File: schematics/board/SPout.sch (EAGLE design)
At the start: 38 parts

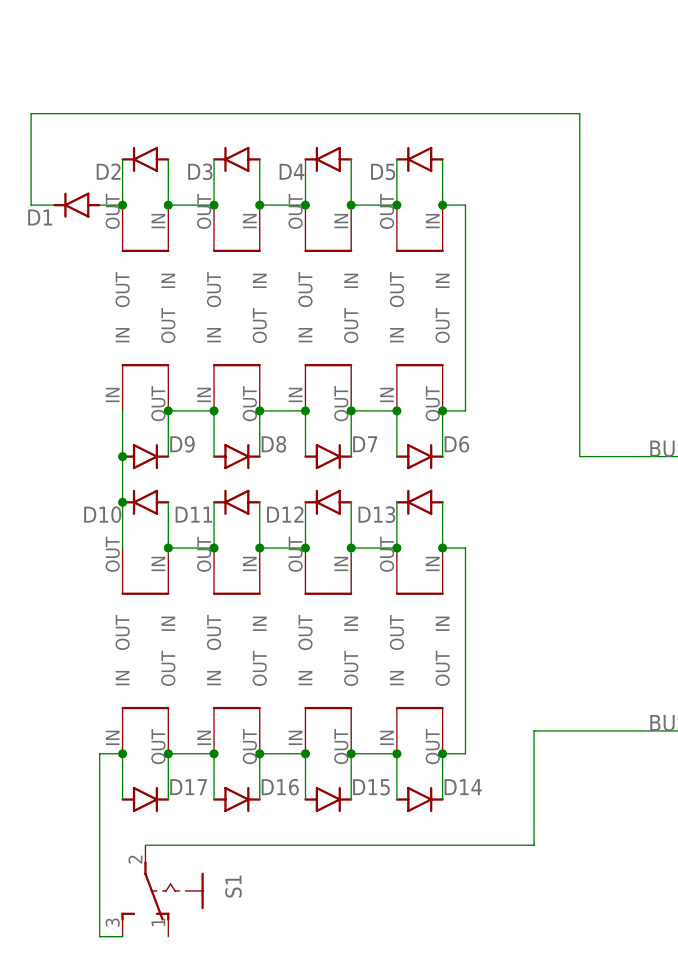
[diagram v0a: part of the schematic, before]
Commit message: Плата СП изменена для возможности подключения 2 вариантов ФЭПов
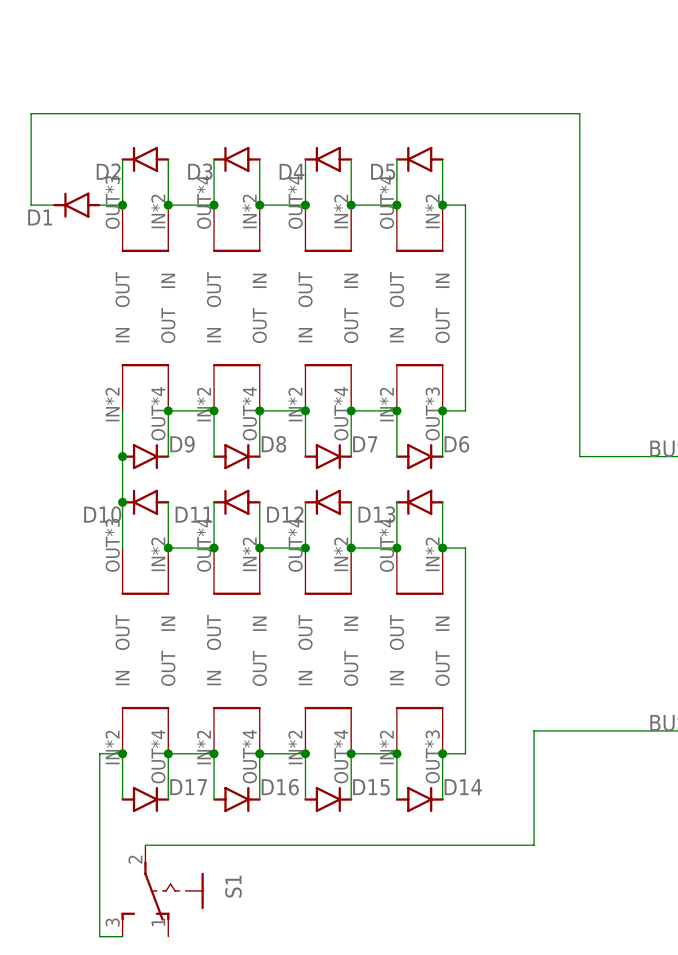
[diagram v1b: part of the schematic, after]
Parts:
- SOL1, SOL10, SOL11, SOL13, SOL14, SOL15, SOL2, SOL3, SOL5, SOL6, SOL7, SOL9: value SOLAR_0 -> SOLAR-2_0; device CanCubeSat:SOLAR_0 -> CanCubeSat:SOLAR-2_0
- SOL12, SOL16, SOL4, SOL8: value SOLAR_1 -> SOLAR-2_1; device CanCubeSat:SOLAR_1 -> CanCubeSat:SOLAR-2_1
- U$6: value GRAFITGRAFIT3_1 -> GRAFITGRAFIT4_2; device CanCubeSat:GRAFITGRAFIT3_1 -> CanCubeSat:GRAFITGRAFIT4_2
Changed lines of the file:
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@@
 <parts>
 <part name="D1" library="diode" library_urn="urn:adsk.eagle:library:210" deviceset="MBR0520LT" device="" package3d_urn="urn:adsk.eagle:package:43420/1"/>
-<part name="SOL1" library="CanCubeSat" deviceset="SOLAR" device="_0"/>
-<part name="SOL2" library="CanCubeSat" deviceset="SOLAR" device="_0"/>
-<part name="SOL3" library="CanCubeSat" deviceset="SOLAR" device="_0"/>
-<part name="SOL5" library="CanCubeSat" deviceset="SOLAR" device="_0"/>
-<part name="SOL6" library="CanCubeSat" deviceset="SOLAR" device="_0"/>
-<part name="SOL7" library="CanCubeSat" deviceset="SOLAR" device="_0"/>
-<part name="SOL9" library="CanCubeSat" deviceset="SOLAR" device="_0"/>
-<part name="SOL10" library="CanCubeSat" deviceset="SOLAR" device="_0"/>
-<part name="SOL11" library="CanCubeSat" deviceset="SOLAR" device="_0"/>
-<part name="SOL13" library="CanCubeSat" deviceset="SOLAR" device="_0"/>
-<part name="SOL14" library="CanCubeSat" deviceset="SOLAR" device="_0"/>
-<part name="SOL15" library="CanCubeSat" deviceset="SOLAR" device="_0"/>
-<part name="SOL16" library="CanCubeSat" deviceset="SOLAR" device="_1"/>
-<part name="SOL12" library="CanCubeSat" deviceset="SOLAR" device="_1"/>
-<part name="SOL8" library="CanCubeSat" deviceset="SOLAR" device="_1"/>
-<part name="SOL4" library="CanCubeSat" deviceset="SOLAR" device="_1"/>
+<part name="SOL1" library="CanCubeSat" deviceset="SOLAR-2" device="_0"/>
+<part name="SOL2" library="CanCubeSat" deviceset="SOLAR-2" device="_0"/>
+<part name="SOL3" library="CanCubeSat" deviceset="SOLAR-2" device="_0"/>
+<part name="SOL5" library="CanCubeSat" deviceset="SOLAR-2" device="_0"/>
+<part name="SOL6" library="CanCubeSat" deviceset="SOLAR-2" device="_0"/>
+<part name="SOL7" library="CanCubeSat" deviceset="SOLAR-2" device="_0"/>
+<part name="SOL9" library="CanCubeSat" deviceset="SOLAR-2" device="_0"/>
+<part name="SOL10" library="CanCubeSat" deviceset="SOLAR-2" device="_0"/>
+<part name="SOL11" library="CanCubeSat" deviceset="SOLAR-2" device="_0"/>
+<part name="SOL13" library="CanCubeSat" deviceset="SOLAR-2" device="_0"/>
+<part name="SOL14" library="CanCubeSat" deviceset="SOLAR-2" device="_0"/>
+<part name="SOL15" library="CanCubeSat" deviceset="SOLAR-2" device="_0"/>
+<part name="SOL16" library="CanCubeSat" deviceset="SOLAR-2" device="_1"/>
+<part name="SOL12" library="CanCubeSat" deviceset="SOLAR-2" device="_1"/>
+<part name="SOL8" library="CanCubeSat" deviceset="SOLAR-2" device="_1"/>
+<part name="SOL4" library="CanCubeSat" deviceset="SOLAR-2" device="_1"/>
 <part name="S1" library="CanCubeSat" deviceset="255SB" device="" package3d_urn="urn:adsk.eagle:package:27679/1"/>
 <part name="R1_2K7" library="rcl" library_urn="urn:adsk.eagle:library:334" deviceset="R-US_" device="R0603" package3d_urn="urn:adsk.eagle:package:23555/3" value="2k7"/>
@@
 <part name="D16" library="diode" library_urn="urn:adsk.eagle:library:210" deviceset="MBR0520LT" device="" package3d_urn="urn:adsk.eagle:package:43420/1"/>
 <part name="D17" library="diode" library_urn="urn:adsk.eagle:library:210" deviceset="MBR0520LT" device="" package3d_urn="urn:adsk.eagle:package:43420/1"/>
-<part name="U$6" library="CanCubeSat" deviceset="GRAFIT" device="GRAFIT3_1"/>
+<part name="U$6" library="CanCubeSat" deviceset="GRAFIT" device="GRAFIT4_2" value="GRAFITGRAFIT4_2"/>
 </parts>
 <sheets>

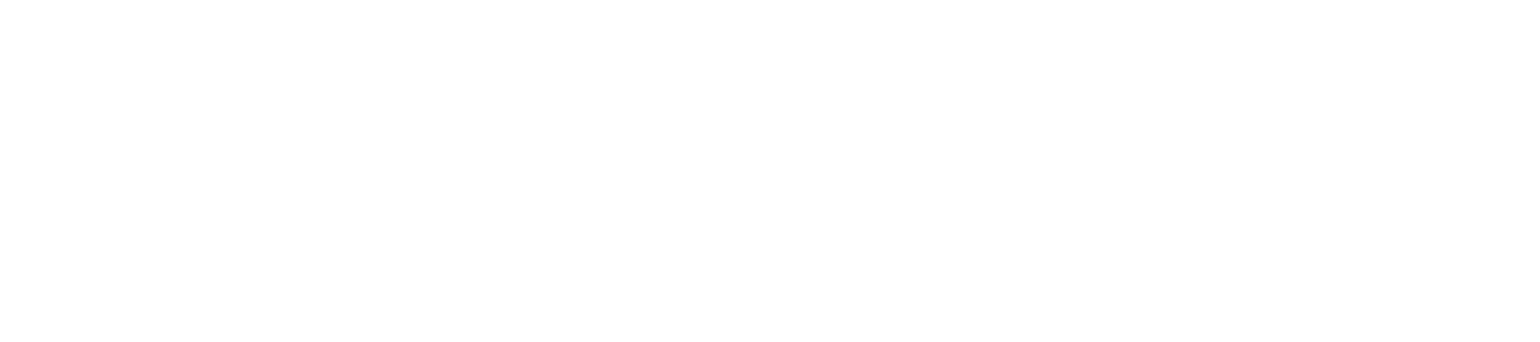
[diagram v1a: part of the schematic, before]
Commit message: Добавлены подписи Концерна к платам
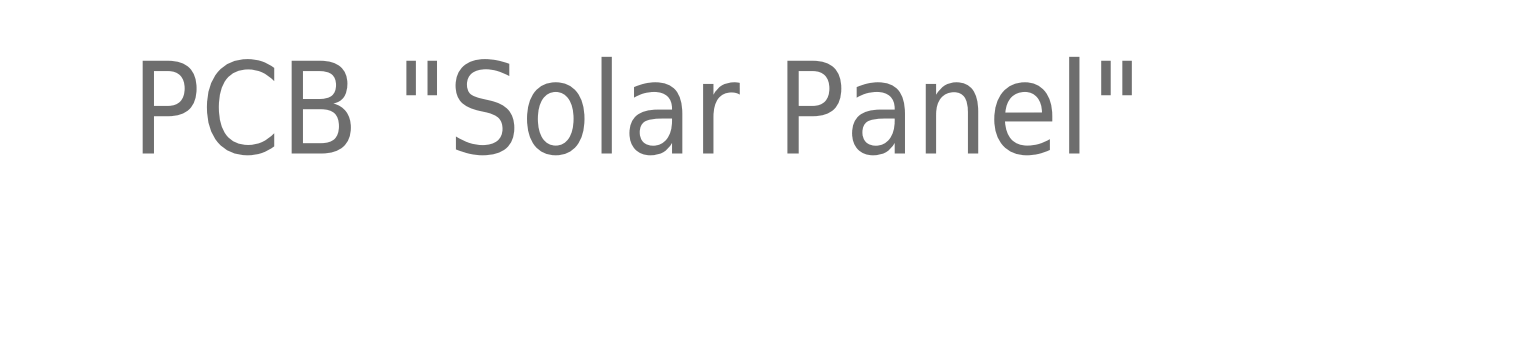
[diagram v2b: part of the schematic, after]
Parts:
- added U$26: PCB "Solar Panel", CanCubeSat:ITS-LOGOPCB-""
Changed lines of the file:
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@@
 <drawing>
 <settings>
-<setting alwaysvectorfont="no"/>
+<setting alwaysvectorfont="yes"/>
 <setting verticaltext="up"/>
 </settings>
@@
 <part name="D17" library="diode" library_urn="urn:adsk.eagle:library:210" deviceset="MBR0520LT" device="" package3d_urn="urn:adsk.eagle:package:43420/1"/>
 <part name="U$6" library="CanCubeSat" deviceset="GRAFIT" device="GRAFIT4_2" value="GRAFITGRAFIT4_2"/>
+<part name="U$26" library="CanCubeSat" deviceset="ITS-LOGO" device="PCB-&quot;&quot;" value="PCB &quot;Solar Panel&quot;"/>
 </parts>
 <sheets>
@@
 </instance>
 <instance part="U$6" gate="G$1" x="144.78" y="231.14" smashed="yes" rot="R90"/>
+<instance part="U$26" gate="G$1" x="30.48" y="312.42" smashed="yes">
+<attribute name="VALUE" x="157.48" y="312.42" size="12.7" layer="96"/>
+</instance>
 </instances>
 <busses>

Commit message: Добавлен конденсатор на питание СБ
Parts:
- added C1: 47µ, rcl:C-EUC1210
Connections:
- net BUS+: now also C1.2
- net BUS-: now also C1.1
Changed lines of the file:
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@@
 <part name="U$6" library="CanCubeSat" deviceset="GRAFIT" device="GRAFIT4_2" value="GRAFITGRAFIT4_2"/>
 <part name="U$26" library="CanCubeSat" deviceset="ITS-LOGO" device="PCB-&quot;&quot;" value="PCB &quot;Solar Panel&quot;"/>
+<part name="C1" library="rcl" library_urn="urn:adsk.eagle:library:334" deviceset="C-EU" device="C1210" package3d_urn="urn:adsk.eagle:package:23619/2" value="47µ"/>
 </parts>
 <sheets>
@@
 <attribute name="VALUE" x="157.48" y="312.42" size="12.7" layer="96"/>
 </instance>
+<instance part="C1" gate="G$1" x="139.7" y="132.08" smashed="yes">
+<attribute name="NAME" x="141.224" y="132.461" size="1.778" layer="95"/>
+<attribute name="VALUE" x="141.224" y="127.381" size="1.778" layer="96"/>
+</instance>
 </instances>
 <busses>
@@
 <segment>
 <label x="127" y="114.3" size="1.778" layer="95"/>
-<wire x1="114.3" y1="114.3" x2="152.4" y2="114.3" width="0.1524" layer="91"/>
+<wire x1="114.3" y1="114.3" x2="139.7" y2="114.3" width="0.1524" layer="91"/>
 <pinref part="S1" gate="1" pin="P"/>
 <pinref part="JP1" gate="G$1" pin="2"/>
+<wire x1="139.7" y1="114.3" x2="152.4" y2="114.3" width="0.1524" layer="91"/>
 <wire x1="160.02" y1="129.54" x2="165.1" y2="129.54" width="0.1524" layer="91"/>
 <wire x1="160.02" y1="114.3" x2="160.02" y2="129.54" width="0.1524" layer="91"/>
@@
 <wire x1="71.12" y1="101.6" x2="114.3" y2="101.6" width="0.1524" layer="91"/>
 <wire x1="114.3" y1="101.6" x2="114.3" y2="114.3" width="0.1524" layer="91"/>
+<pinref part="C1" gate="G$1" pin="2"/>
+<wire x1="139.7" y1="127" x2="139.7" y2="114.3" width="0.1524" layer="91"/>
+<junction x="139.7" y="114.3"/>
 </segment>
 </net>
@@
 <wire x1="160.02" y1="144.78" x2="160.02" y2="132.08" width="0.1524" layer="91"/>
 <wire x1="160.02" y1="132.08" x2="165.1" y2="132.08" width="0.1524" layer="91"/>
-<wire x1="152.4" y1="144.78" x2="119.38" y2="144.78" width="0.1524" layer="91"/>
+<wire x1="152.4" y1="144.78" x2="139.7" y2="144.78" width="0.1524" layer="91"/>
 <label x="127" y="144.78" size="1.778" layer="95"/>
+<wire x1="139.7" y1="144.78" x2="119.38" y2="144.78" width="0.1524" layer="91"/>
 <wire x1="160.02" y1="144.78" x2="152.4" y2="144.78" width="0.1524" layer="91"/>
 <wire x1="119.38" y1="182.88" x2="119.38" y2="144.78" width="0.1524" layer="91"/>
@@
 <wire x1="152.4" y1="142.24" x2="152.4" y2="144.78" width="0.1524" layer="91"/>
 <junction x="152.4" y="144.78"/>
-</segment>
-</net>
+<pinref part="C1" gate="G$1" pin="1"/>
+<wire x1="139.7" y1="134.62" x2="139.7" y2="144.78" width="0.1524" layer="91"/>
+<junction x="139.7" y="144.78"/>
+</segment>
+</net>

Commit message: Добавлена шелкография на платах БСК и СП
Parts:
- renumbered R1_2K7 to 2K7
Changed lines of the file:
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@@
 <part name="SOL4" library="CanCubeSat" deviceset="SOLAR-2" device="_1"/>
 <part name="S1" library="CanCubeSat" deviceset="255SB" device="" package3d_urn="urn:adsk.eagle:package:27679/1"/>
-<part name="R1_2K7" library="rcl" library_urn="urn:adsk.eagle:library:334" deviceset="R-US_" device="R0603" package3d_urn="urn:adsk.eagle:package:23555/3" value="2k7"/>
+<part name="2K7" library="rcl" library_urn="urn:adsk.eagle:library:334" deviceset="R-US_" device="R0603" package3d_urn="urn:adsk.eagle:package:23555/3" value="2k7"/>
 <part name="PWR" library="led" library_urn="urn:adsk.eagle:library:259" deviceset="LED" device="CHIPLED_0603" package3d_urn="urn:adsk.eagle:package:15822/2"/>
 <part name="JP1" library="pinhead" library_urn="urn:adsk.eagle:library:325" deviceset="PINHD-1X2" device="" package3d_urn="urn:adsk.eagle:package:22435/2"/>
@@
 <attribute name="VALUE" x="77.47" y="93.345" size="1.778" layer="96" rot="R270"/>
 </instance>
-<instance part="R1_2K7" gate="G$1" x="152.4" y="124.46" smashed="yes" rot="R90">
+<instance part="2K7" gate="G$1" x="152.4" y="124.46" smashed="yes" rot="R90">
 <attribute name="NAME" x="150.9014" y="120.65" size="1.778" layer="95" rot="R90"/>
 <attribute name="VALUE" x="155.702" y="120.65" size="1.778" layer="96" rot="R90"/>
@@
 <wire x1="160.02" y1="129.54" x2="165.1" y2="129.54" width="0.1524" layer="91"/>
 <wire x1="160.02" y1="114.3" x2="160.02" y2="129.54" width="0.1524" layer="91"/>
-<pinref part="R1_2K7" gate="G$1" pin="1"/>
+<pinref part="2K7" gate="G$1" pin="1"/>
 <wire x1="152.4" y1="114.3" x2="160.02" y2="114.3" width="0.1524" layer="91"/>
 <wire x1="152.4" y1="119.38" x2="152.4" y2="114.3" width="0.1524" layer="91"/>
@@
 <segment>
 <pinref part="PWR" gate="G$1" pin="A"/>
-<pinref part="R1_2K7" gate="G$1" pin="2"/>
+<pinref part="2K7" gate="G$1" pin="2"/>
 <wire x1="152.4" y1="134.62" x2="152.4" y2="129.54" width="0.1524" layer="91"/>
 </segment>
